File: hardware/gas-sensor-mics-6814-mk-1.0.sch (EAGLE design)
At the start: 7 parts, among them U1 MICS-6814

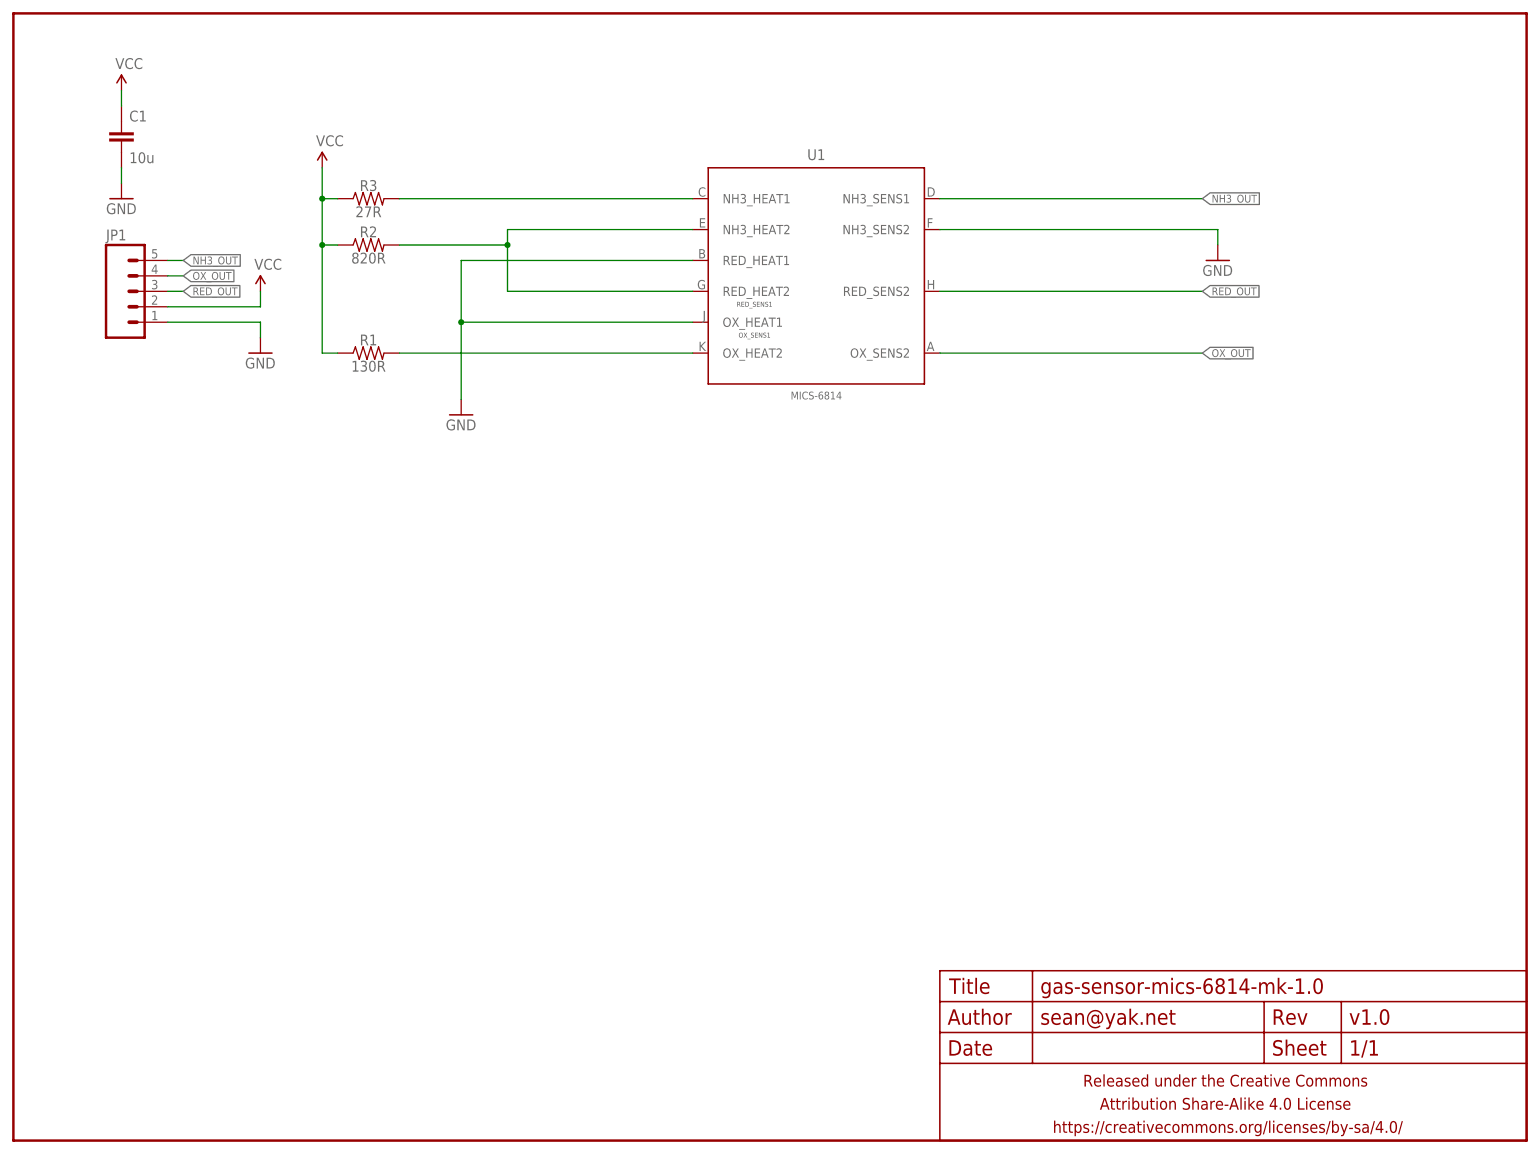
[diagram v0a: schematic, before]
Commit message: gas sensor test boards
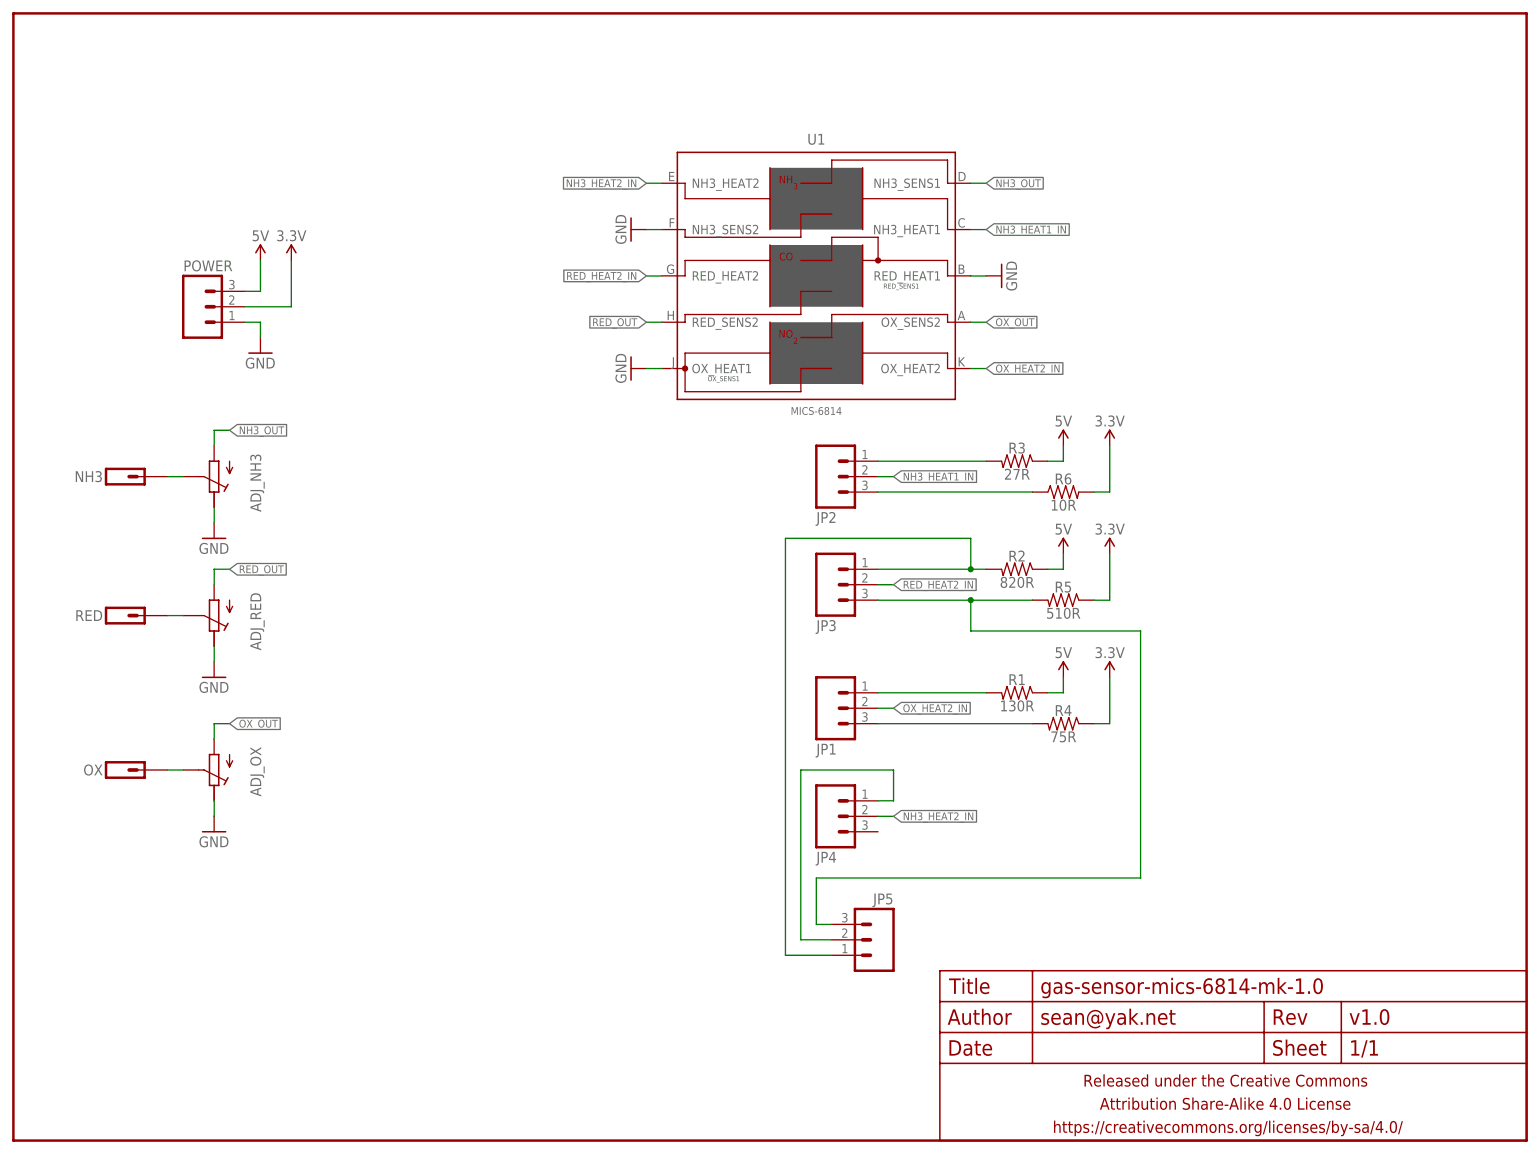
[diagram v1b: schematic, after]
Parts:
- removed C1: 10u, a_parts:CAPACITOR-CERAMICC0805
- added ADJ_NH3, ADJ_OX, ADJ_RED: (no value), a_parts:POTENTIOMETEREVM3Y
- added JP2, JP3, JP4, JP5, POWER: M03PTH-CENTERED, a_parts:M03PTH-CENTERED
- added NH3, OX, RED: M01PTH-2MM-OFFSET, a_parts:M01PTH-2MM-OFFSET
- added R4: 75R, a_parts:RESISTORR0603-TIGHTER
- added R5: 510R, a_parts:RESISTORR0603-TIGHTER
- added R6: 10R, a_parts:RESISTORR0603-TIGHTER
- JP1: value M05PTH-CENTERED -> M03PTH-CENTERED; device a_parts:M05PTH-CENTERED -> a_parts:M03PTH-CENTERED
- R1, R2, R3: device a_parts:RESISTORR0805 -> a_parts:RESISTORR0603-TIGHTER
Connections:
- removed net N$4: R2.2, U1.NH3_HEAT2, U1.RED_HEAT2
- removed net VCC: C1.1, JP1.2, R1.1, R2.1, R3.1
- new net 3.3V: POWER.2, R4.1, R5.1, R6.2
- new net 5V: POWER.3, R1.1, R2.1, R3.1
- new net N$11: JP3.3, JP5.3, R5.2
- new net N$12: JP3.1, JP5.1, R2.2
- new net N$13: JP4.1, JP5.2
- new net N$2: ADJ_NH3.S, NH3.1
- new net N$3: ADJ_RED.S, RED.1
- new net N$5: ADJ_OX.S, OX.1
- new net N$7: JP1.3, R4.2
- new net N$8: JP2.3, R6.1
- new net NH3_HEAT1_IN: JP2.2, U1.NH3_HEAT1
- new net NH3_HEAT2_IN: JP4.2, U1.NH3_HEAT2
- new net OX_HEAT2_IN: JP1.2, U1.OX_HEAT2
- new net RED_HEAT2_IN: JP3.2, U1.RED_HEAT2
- net GND: now also ADJ_NH3.E, ADJ_OX.E, ADJ_RED.E, POWER.1; no longer C1.2, JP1.1
- net N$1: now also JP2.1; no longer U1.NH3_HEAT1
- net N$6: now also JP1.1; no longer U1.OX_HEAT2
- net NH3_OUT: now also ADJ_NH3.A; no longer JP1.5
- net OX_OUT: now also ADJ_OX.A; no longer JP1.4
- net RED_OUT: now also ADJ_RED.A; no longer JP1.3
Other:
- moved on the sheet: R1, R2, R3
